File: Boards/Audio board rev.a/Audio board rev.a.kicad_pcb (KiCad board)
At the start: 2 copper layers, 187.4 x 165.9 mm, 78 parts, among them J1 CEC card edge connector large, U1 6821, U10 LM324, U11 MC1458, U2 LM339, U3 LM339, U4 ULN2003A, U5 DAC-08, U6 DAC-08, U7 AH5012, U9 LM324

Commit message: U7/U9 area laid out, best guess on 0.025" grid for silk, 0.05" grid for parts
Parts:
- added C1: 4.7uF, Evan's parts:CP_Radial_Tantal_D4mm_P3.81mm, F.Cu at (213.4, 188.0)
- added C10: 10uF, Evan's parts:CP_Axial_L10.0mm_D4.5mm_P27.94mm_Horizontal, F.Cu at (106.4, 161.2)
- added C19: 100pF, Capacitor_THT:C_Rect_L7.0mm_W2.5mm_P5.00mm, F.Cu at (172.7, 85.2)
- added C2: 4.7uF, Evan's parts:CP_Radial_Tantal_D4mm_P3.81mm, F.Cu at (218.4, 132.1)
- added C20: 100pF, Capacitor_THT:C_Rect_L7.0mm_W2.5mm_P5.00mm, F.Cu at (184.8, 157.4)
- added C21: 4.7uF, Evan's parts:CP_Radial_Tantal_D4mm_P3.81mm, F.Cu at (175.3, 168.9)
- added C22: 100pF, Capacitor_THT:C_Rect_L7.0mm_W2.5mm_P5.00mm, F.Cu at (172.7, 110.6)
- added C23: 100pF, Capacitor_THT:C_Rect_L7.0mm_W2.5mm_P5.00mm, F.Cu at (191.1, 157.4)
- added C24: 4.7uF, Evan's parts:CP_Radial_Tantal_D4mm_P3.81mm, F.Cu at (200.7, 168.9)
- added C25: 100pF, Capacitor_THT:C_Rect_L7.0mm_W2.5mm_P5.00mm, F.Cu at (190.5, 188.0)
- added C3: 4.7uF, Evan's parts:CP_Radial_Tantal_D4mm_P3.81mm, F.Cu at (218.4, 138.4)
- added C36: 10nF, Capacitor_THT:C_Disc_D3.0mm_W1.6mm_P2.50mm, F.Cu at (177.8, 149.9)
- added C37: 10nF, Capacitor_THT:C_Disc_D3.0mm_W1.6mm_P2.50mm, F.Cu at (195.6, 149.9)
- added C7: 220pF, Capacitor_THT:C_Rect_L7.0mm_W2.5mm_P5.00mm, F.Cu at (139.1, 201.9)
- added C9: 10pF, Capacitor_THT:C_Rect_L7.0mm_W2.5mm_P5.00mm, F.Cu at (113.0, 171.4)
- added DS1: LED, LED_THT:LED_D5.0mm_Horizontal_O3.81mm_Z15.0mm, F.Cu at (59.7, 116.8)
- added DS2: LED, LED_THT:LED_D5.0mm_Horizontal_O3.81mm_Z15.0mm, F.Cu at (59.7, 110.5)
- added DS3: LED, LED_THT:LED_D5.0mm_Horizontal_O3.81mm_Z15.0mm, F.Cu at (59.7, 104.1)
- added DS4: LED, LED_THT:LED_D5.0mm_Horizontal_O3.81mm_Z15.0mm, F.Cu at (59.7, 97.8)
- added DS5: LED, LED_THT:LED_D5.0mm_Horizontal_O3.81mm_Z15.0mm, F.Cu at (59.7, 91.4)
- added DS6: LED, LED_THT:LED_D5.0mm_Horizontal_O3.81mm_Z15.0mm, F.Cu at (59.7, 85.1)
- added DS7: LED, LED_THT:LED_D5.0mm_Horizontal_O3.81mm_Z15.0mm, F.Cu at (59.7, 78.7)
- added R19: 100K, Potentiometer_THT:Potentiometer_Bourns_3005_Horizontal, F.Cu at (71.1, 175.3)
- added R34: 100K, Potentiometer_THT:Potentiometer_Bourns_3005_Horizontal, F.Cu at (71.1, 170.2)
- added R36: 100K, Potentiometer_THT:Potentiometer_Bourns_3005_Horizontal, F.Cu at (71.1, 67.3)
- added R38: 100K, Potentiometer_THT:Potentiometer_Bourns_3005_Horizontal, F.Cu at (71.1, 72.4)
- CR3, CR4: footprint Diode_THT:D_DO-35_SOD27_P7.62mm_Horizontal -> Diode_THT:D_DO-34_SOD68_P12.70mm_Horizontal
- R1, R10, R11, R12, R13, R14, R15, R16, R17, R18, R2, R20, R21, R22, R23, R24, R25, R26, R27, R28, R29, R3, R30, R31, R32, R33, R35, R37, R39, R4, R40, R41, R42, R43, R5, R6, R7, R8, R9: footprint Resistor_THT:R_Axial_DIN0309_L9.0mm_D3.2mm_P12.70mm_Horizontal -> Evan's parts:R_Axial_DIN0204_L3.6mm_D1.6mm_P12.7mm_Horizontal
- moved R31 425.8 mm to (195.6, 182.9), turned to -90 degrees
- moved R1 425.2 mm to (205.7, 43.2), turned to 180 degrees
- moved R30 421.1 mm to (198.1, 162.6), turned to 90 degrees
- moved R39 421.0 mm to (200.7, 185.4), turned to 90 degrees
- moved R29 420.9 mm to (195.6, 162.6), turned to 90 degrees
- moved U1 417.7 mm to (148.6, 67.3), turned to 90 degrees
- moved CR3 416.4 mm to (120.7, 175.3), turned to 90 degrees
- moved R32 413.8 mm to (180.3, 190.5), turned to 90 degrees
- moved CR4 412.4 mm to (118.1, 175.3), turned to 90 degrees
- moved R41 412.1 mm to (204.5, 162.6), turned to 90 degrees
- moved R25 408.1 mm to (194.9, 130.8), turned to 180 degrees
- moved R28 407.3 mm to (177.8, 162.6), turned to 90 degrees
- moved R33 407.1 mm to (175.3, 190.5), turned to 90 degrees
- moved R24 403.9 mm to (196.8, 101.6), turned to 180 degrees
- moved U7 401.4 mm to (179.7, 146.1), turned to 90 degrees
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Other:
- board size 187.4 x 165.9 mm -> 165.9 x 187.4 mm
- board text added: "AC"
- board text added: "DC"
- board text added: "MIKE"

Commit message: initial placement of components done
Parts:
- moved C14 19.1 mm to (121.9, 109.2), turned to 180 degrees
- moved R37 18.8 mm to (138.4, 48.3)
- moved R22 18.3 mm to (125.7, 63.5)
- moved R20 18.3 mm to (133.3, 63.5)
- moved U11 16.3 mm to (125.7, 55.9)
- moved C9 16.0 mm to (120.7, 157.4)
- moved R21 14.4 mm to (129.5, 71.1)
- moved R18 14.2 mm to (119.4, 176.5)
- moved R17 13.7 mm to (121.9, 176.5)
- moved C8 13.1 mm to (144.8, 154.9)
- moved C12 12.7 mm to (121.9, 106.7), turned to 180 degrees
- moved C17 12.0 mm to (121.9, 127.0), turned to 180 degrees
- moved R12 12.0 mm to (142.2, 190.5)
- moved R14 12.0 mm to (142.2, 154.9)
- moved R15 12.0 mm to (132.1, 162.6)
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
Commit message: most of layout done, fixed some bugs
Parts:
- moved R10 10.2 mm to (142.2, 137.2), turned to 180 degrees
- moved R39 8.91 mm to (200.0, 176.5), turned to -90 degrees
- moved R29 7.65 mm to (194.9, 154.9), turned to -90 degrees
- moved R27 7.65 mm to (179.7, 154.9), turned to -90 degrees
- moved R30 7.65 mm to (197.5, 154.9), turned to -90 degrees
- moved R40 7.65 mm to (170.8, 182.9), turned to -90 degrees
- moved R41 7.65 mm to (203.8, 154.9), turned to -90 degrees
- moved R42 7.65 mm to (170.8, 154.9), turned to -90 degrees
- moved R6 7.62 mm to (149.2, 124.5), turned to -90 degrees
- moved R8 7.62 mm to (154.3, 124.5), turned to -90 degrees
- moved R13 7.62 mm to (139.7, 154.9), turned to -90 degrees
- moved R17 7.62 mm to (121.9, 168.9), turned to -90 degrees
- moved R18 7.62 mm to (119.4, 168.9), turned to -90 degrees
- moved R21 7.62 mm to (129.5, 63.5), turned to -90 degrees
- moved R3 7.62 mm to (151.8, 106.7), turned to -90 degrees
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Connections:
- C21 pad 2: Net-(C21-Pad2) -> Pin 65
- C24 pad 2: Net-(C24-Pad2) -> Pin 64
- R19 pad 1: Net-(U10A--) -> Net-(C10-Pad1)
- R19 pad 3: Net-(C10-Pad1) -> Net-(U10A--)
- R25 pad 1: Net-(C24-Pad2) -> Pin 64
- R25 pad 2: Pin 64 -> Net-(R25-Pad2)
- R26 pad 1: Net-(C21-Pad2) -> Pin 65
- R26 pad 2: Pin 65 -> Net-(R26-Pad2)
- R28 pad 1: Net-(C21-Pad2) -> Pin 65
- R30 pad 2: Net-(C24-Pad2) -> Pin 64
- R38 pad 1: BGIN -> GND
- R38 pad 3: GND -> BGIN
- R39 pad 2: Net-(U9B--) -> Net-(C25-Pad1)
- U1 pad 18: CB1 -> unconnected-(U1-CB1-Pad18)
- U1 pad 39: unconnected-(U1-CA2-Pad39) -> CA2
- U7 pad 11: Pin 64 -> Net-(R25-Pad2)
- U7 pad 14: Pin 65 -> Net-(R26-Pad2)
- U7 pad 15: CB1 -> CA2
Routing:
- net GND: track 0.00 -> 579.5 mm, vias 0 -> 10
- net +12V: track 0.00 -> 564.3 mm, vias 0 -> 6
- net -12V: track 0.00 -> 545.5 mm, vias 0 -> 5
- net +5V: track 0.00 -> 490.4 mm, vias 0 -> 2
- net Pin 65: track 0.00 -> 307.6 mm, vias 0 -> 2
- net BGOUT: track 0.00 -> 277.5 mm, vias 0 -> 4
- net BGIN: track 0.00 -> 269.4 mm, vias 0 -> 3
- net AUDOUT: track 0.00 -> 207.6 mm, vias 0 -> 2
- net MIKEIN: track 0.00 -> 185.6 mm, vias 0 -> 3
- net Net-(R34-Pad3): track 0.00 -> 181.3 mm, vias 0 -> 1
- net Pin 64: track 0.00 -> 169.6 mm, vias 0 -> 3
- net Net-(R33-Pad1): track 0.00 -> 135.0 mm
- net Net-(C10-Pad1): track 0.00 -> 134.1 mm
- net Net-(U9B--): track 0.00 -> 119.0 mm, vias 0 -> 2
- net Net-(R14-Pad2): track 0.00 -> 116.1 mm, vias 0 -> 1
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
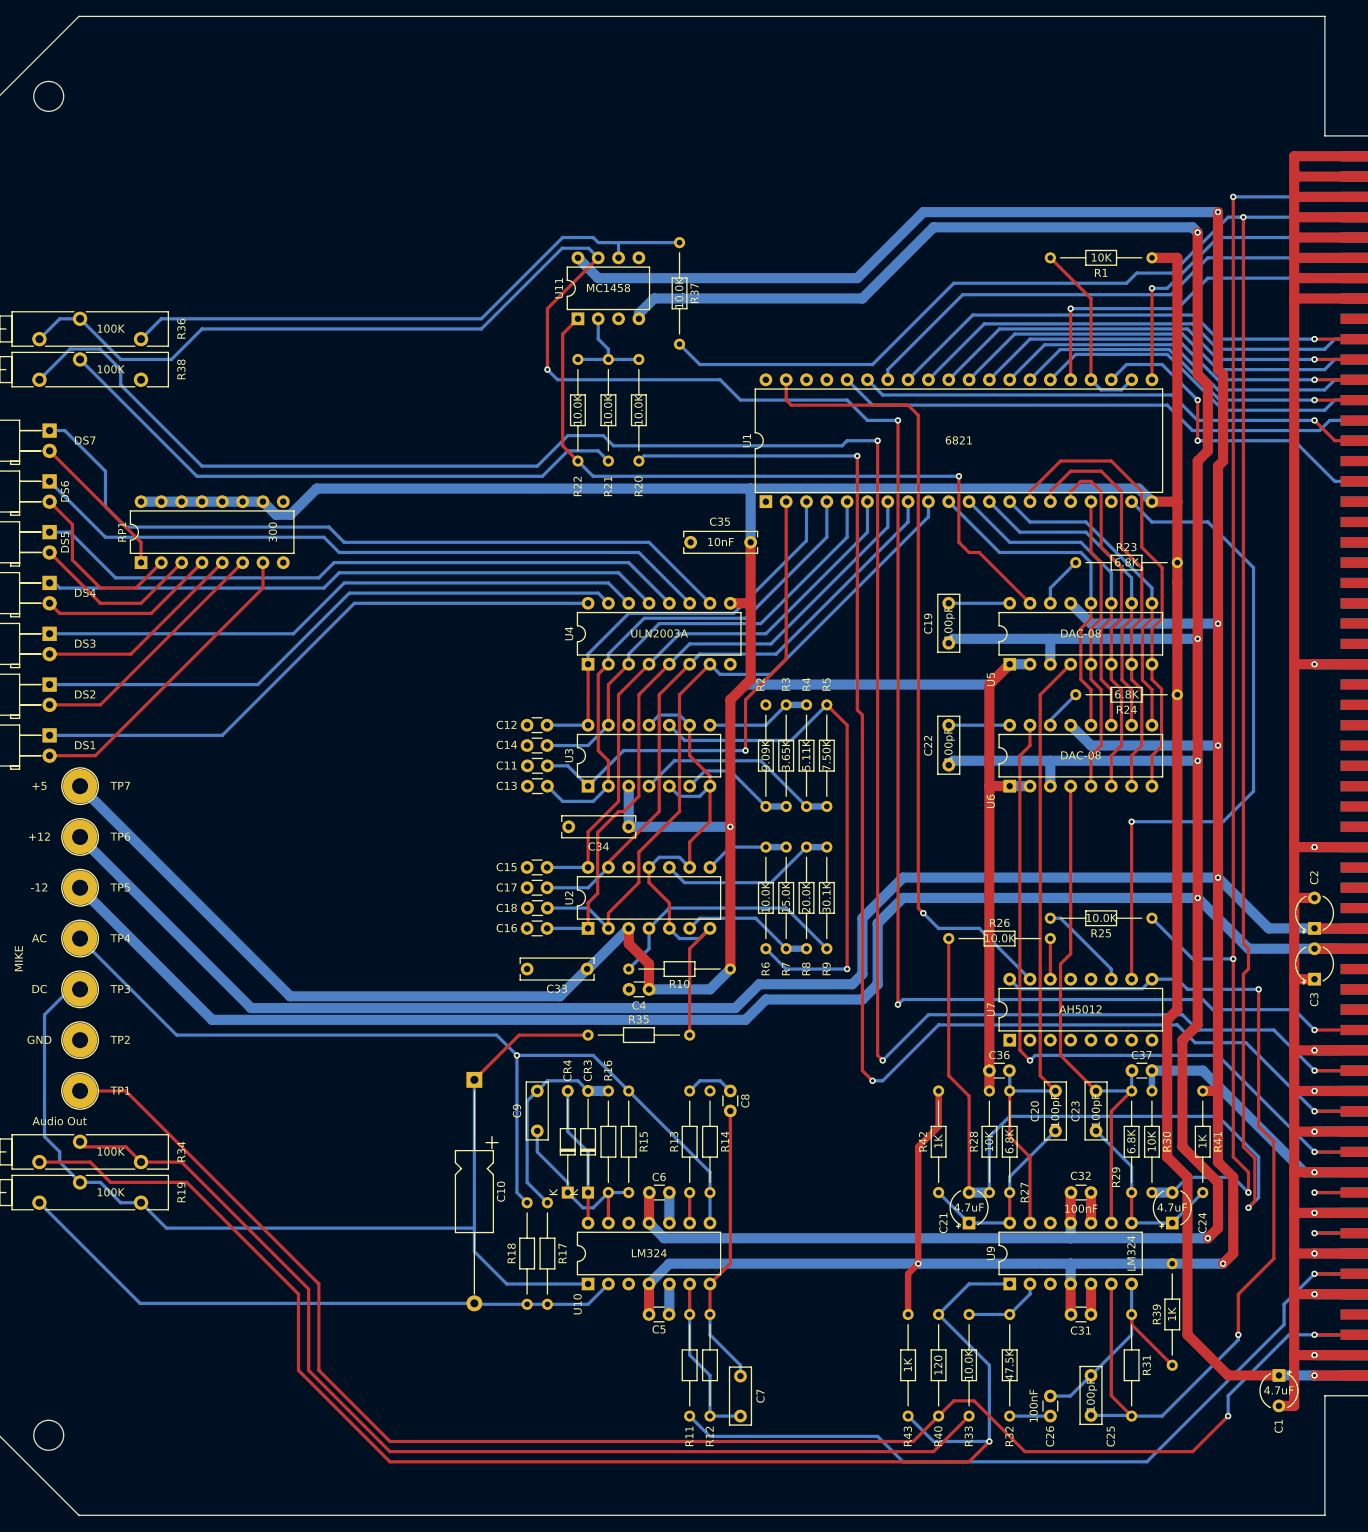
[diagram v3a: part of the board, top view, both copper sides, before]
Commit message: front copper fill done
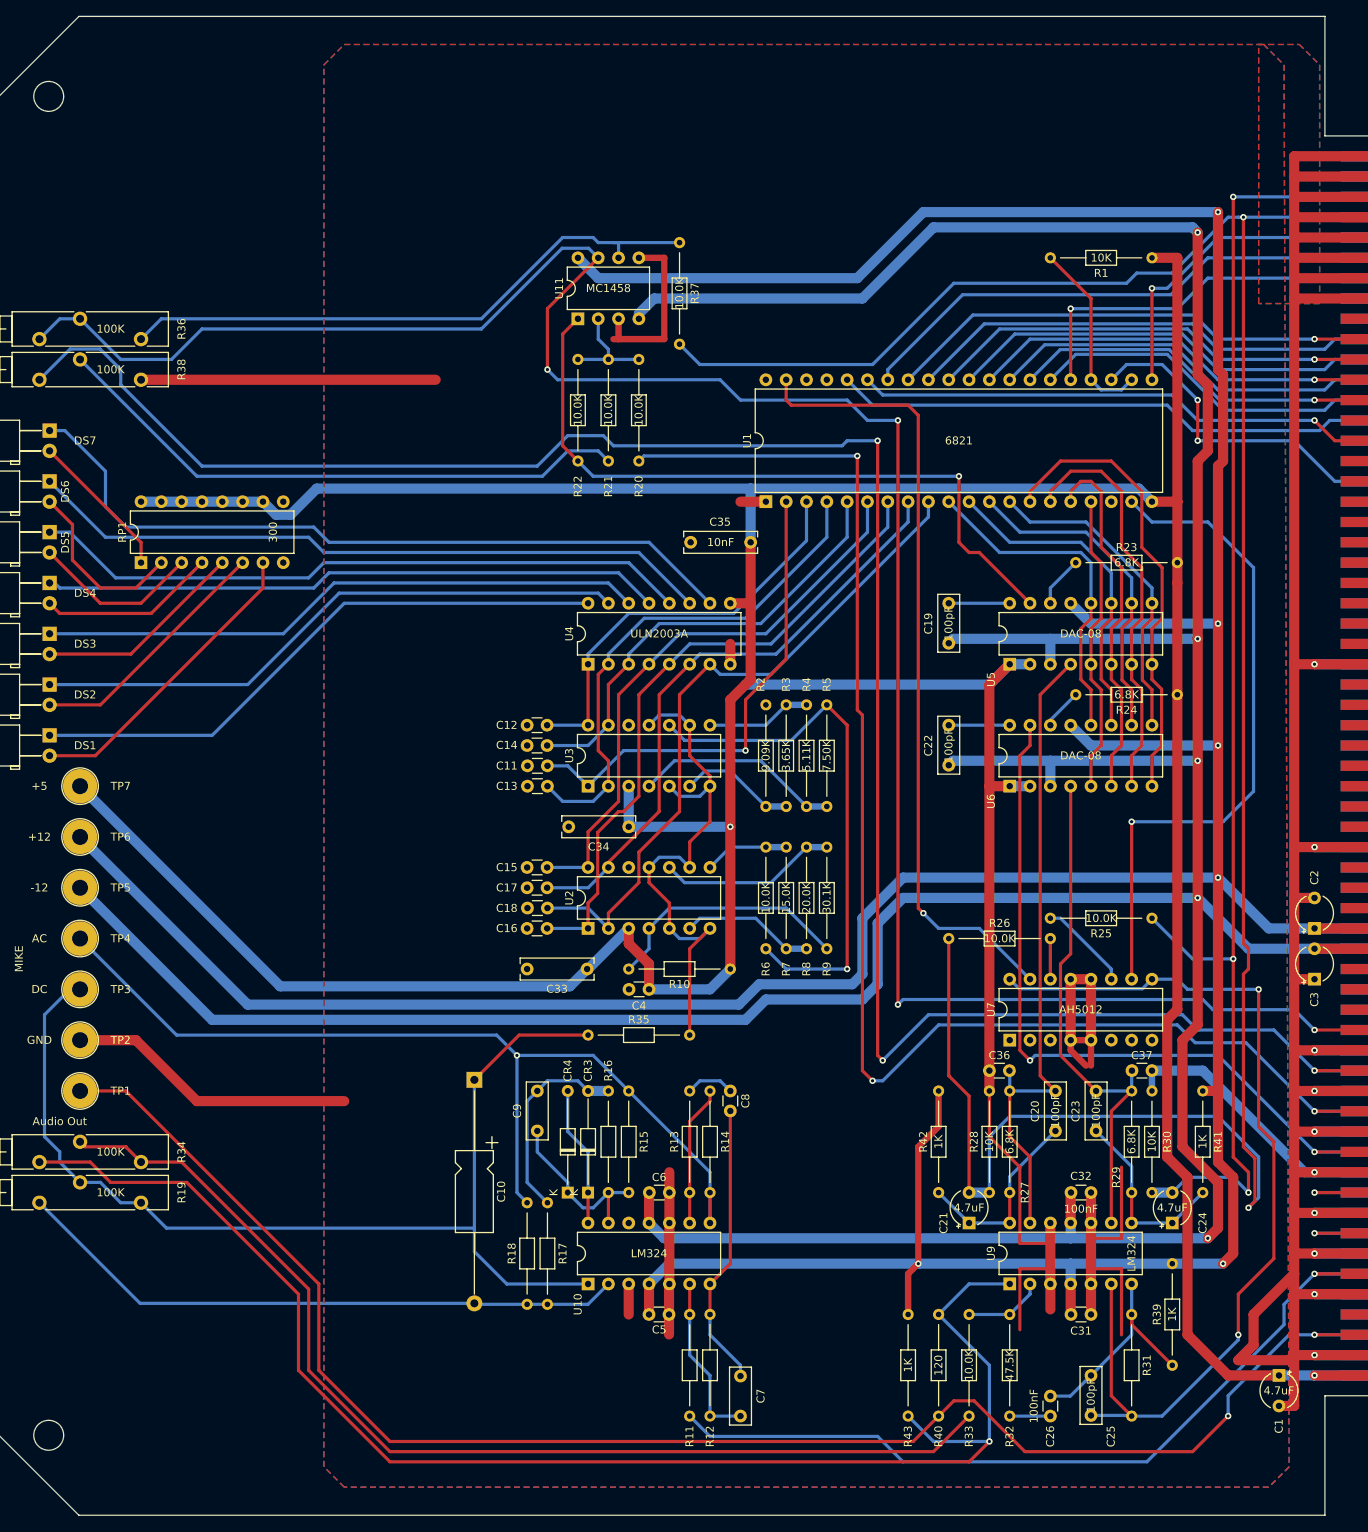
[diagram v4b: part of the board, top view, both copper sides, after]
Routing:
- net GND: track 579.5 -> 830.7 mm
- net Net-(U10C--): track 3.81 -> 17.6 mm
- net Net-(R14-Pad2): track 116.1 -> 119.3 mm
- net +5V: track 490.4 -> 489.4 mm
- added copper zone on B.Cu, net GND
- added copper zone on F.Cu, net GND

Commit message: layout done minus logo
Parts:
- added REF**: MountingHole_3.2mm_M3, MountingHole:MountingHole_3.2mm_M3, F.Cu at (197.5, 27.9)
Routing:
- net GND: track 830.7 -> 877.5 mm
- net Net-(C23-Pad2): track 23.8 -> 27.0 mm
- net Net-(C20-Pad2): track 24.3 -> 27.5 mm
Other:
- board text added: "07-0033 REV A"
- board text added: "122"
- board text added: "62"
- board text added: "AGC"
- board text added: "ASSY 06-0033 ERV A"
- board text added: "AUDIO CONTROL"
- board text added: "GAME RM OUT"
- board text added: "MUSIC IN"
- board text added: "SBC-2A 06-82"

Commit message: layout tweaks to reva
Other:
- board text added: "ASSY 06-0033 REV A"
- board text removed: "ASSY 06-0033 ERV A"
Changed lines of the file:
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@@
     (effects (font (size 1 1) (thickness 0.15)) (justify left bottom))
   )
-  (gr_text "ASSY 06-0033\nERV A" (at 78.74 34.925) (layer "F.SilkS")
+  (gr_text "ASSY 06-0033\nREV A" (at 78.74 34.925) (layer "F.SilkS")
     (effects (font (size 1 1) (thickness 0.15)) (justify left bottom))
   )
@@
   (segment (start 187.325 170.815) (end 136.525 170.815) (width 1.27) (layer "B.Cu") (net 34))
   (segment (start 202.565 44.45) (end 170.18 44.45) (width 1.27) (layer "B.Cu") (net 34))
+  (segment (start 149.225 140.97) (end 146.685 143.51) (width 1.27) (layer "B.Cu") (net 34))
   (segment (start 184.785 95.885) (end 172.64 95.885) (width 1.27) (layer "B.Cu") (net 34))
   (segment (start 172.64 111.125) (end 172.085 111.68) (width 1.27) (layer "B.Cu") (net 34))
-  (segment (start 163.195 139.065) (end 163.195 131.445) (width 1.27) (layer "B.Cu") (net 34))
-  (segment (start 163.195 131.445) (end 166.37 128.27) (width 1.27) (layer "B.Cu") (net 34))
   (segment (start 135.255 53.34) (end 133.35 55.245) (width 1.27) (layer "B.Cu") (net 34))
+  (segment (start 161.925 140.97) (end 149.225 140.97) (width 1.27) (layer "B.Cu") (net 34))
   (segment (start 170.18 44.45) (end 161.29 53.34) (width 1.27) (layer "B.Cu") (net 34))
   (segment (start 184.785 99.06) (end 184.785 95.885) (width 1.27) (layer "B.Cu") (net 34))
   (segment (start 187.325 170.815) (end 187.325 168.9) (width 1.27) (layer "B.Cu") (net 34))
-  (segment (start 63.5 127) (end 80.01 143.51) (width 1.27) (layer "B.Cu") (net 34))
+  (segment (start 163.83 139.065) (end 161.925 140.97) (width 1.27) (layer "B.Cu") (net 34))
   (segment (start 203.2 128.27) (end 209.55 134.62) (width 1.27) (layer "B.Cu") (net 34))
-  (segment (start 166.37 128.27) (end 203.2 128.27) (width 1.27) (layer "B.Cu") (net 34))
-  (segment (start 161.29 140.97) (end 163.195 139.065) (width 1.27) (layer "B.Cu") (net 34))
-  (segment (start 146.685 143.51) (end 149.225 140.97) (width 1.27) (layer "B.Cu") (net 34))
+  (segment (start 80.01 143.51) (end 63.5 127) (width 1.27) (layer "B.Cu") (net 34))
+  (segment (start 163.83 132.08) (end 163.83 139.065) (width 1.27) (layer "B.Cu") (net 34))
+  (segment (start 167.64 128.27) (end 163.83 132.08) (width 1.27) (layer "B.Cu") (net 34))
   (segment (start 226.06 134.62) (end 217.805 134.62) (width 1.27) (layer "B.Cu") (net 34))
   (segment (start 184.785 114.3) (end 184.785 111.125) (width 1.27) (layer "B.Cu") (net 34))
@@
   (segment (start 184.785 111.125) (end 172.64 111.125) (width 1.27) (layer "B.Cu") (net 34))
   (segment (start 161.29 53.34) (end 135.255 53.34) (width 1.27) (layer "B.Cu") (net 34))
+  (segment (start 146.685 143.51) (end 80.01 143.51) (width 1.27) (layer "B.Cu") (net 34))
+  (segment (start 203.2 128.27) (end 167.64 128.27) (width 1.27) (layer "B.Cu") (net 34))
   (segment (start 172.64 95.885) (end 172.085 96.44) (width 1.27) (layer "B.Cu") (net 34))
   (segment (start 184.785 111.125) (end 203.2 111.125) (width 1.27) (layer "B.Cu") (net 34))
   (segment (start 133.35 55.245) (end 133.35 55.88) (width 1.27) (layer "B.Cu") (net 34))
-  (segment (start 149.225 140.97) (end 161.29 140.97) (width 1.27) (layer "B.Cu") (net 34))
-  (segment (start 80.01 143.51) (end 146.685 143.51) (width 1.27) (layer "B.Cu") (net 34))
   (segment (start 203.2 45.085) (end 202.565 44.45) (width 1.27) (layer "B.Cu") (net 34))
   (segment (start 136.525 170.815) (end 134.62 168.91) (width 1.27) (layer "B.Cu") (net 34))
@@
       (pts
         (xy 183.515 43.18)
-        (xy 183.515 43.18)
         (xy 183.515 63.5)
         (xy 149.225 63.5)
@@
         (xy 135.255 57.15)
         (xy 125.73 57.15)
-        (xy 123.825 57.785)
-      )
-    )
+      )
+    )
